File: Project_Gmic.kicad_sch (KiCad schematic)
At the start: 33 parts, among them J1 USB4085-GF-A, J2 SJ1-3523N, SW1 PCM12SMTR, T1 ESMIT-4180/C, U1 TC1055, U2 R05CTE05S

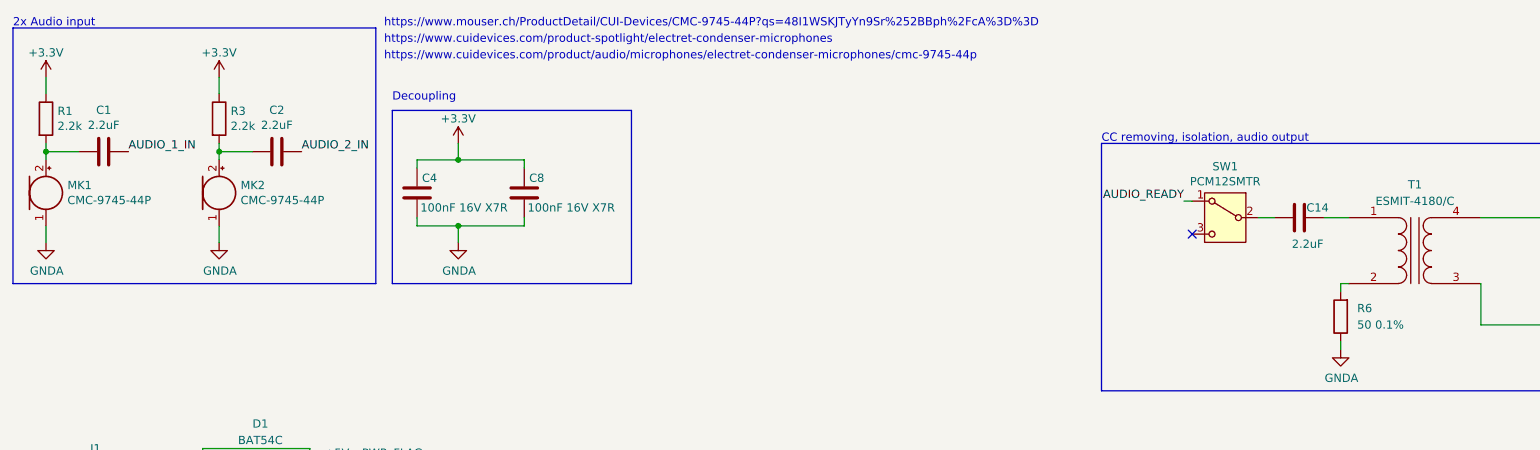
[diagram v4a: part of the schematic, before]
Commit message: placement, BOM inside kicad
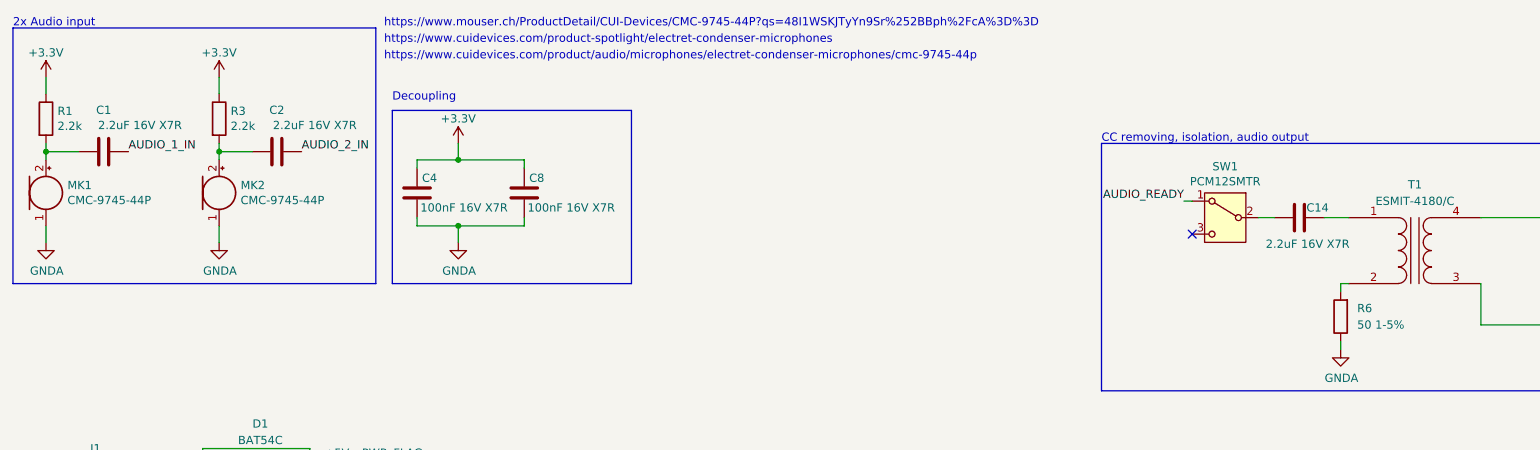
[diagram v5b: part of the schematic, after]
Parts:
- C1, C14, C2: value 2.2uF -> 2.2uF 16V X7R; Manufacturer (none) -> Samsung Electro-Mechanics; Price (none) -> 0.109; Store (none) -> Mouser; StoreID (none) -> 187-CL21B225KOFNNNE
- C10: Manufacturer (none) -> Wurth Elektronik; Price (none) -> 0.091; Store (none) -> Mouser; StoreID (none) -> 710-885012207051
- C11: Manufacturer (none) -> Wurth Elektronik; Price (none) -> 0.053; Store (none) -> Mouser; StoreID (none) -> 710-885012207045
- C12, C3: footprint (none) -> Capacitor_SMD:CP_Elec_4x5.4; Manufacturer (none) -> Wurth Elektronik; Price (none) -> 0.163; Store (none) -> Mouser; StoreID (none) -> 710-865080340001
- C13, C4, C5, C6, C8: footprint (none) -> Capacitor_SMD:C_0805_2012Metric; Manufacturer (none) -> Wurth Elektronik; Price (none) -> 0.053; Store (none) -> Mouser; StoreID (none) -> 710-885012207045
- C7, C9: footprint (none) -> Capacitor_SMD:CP_Elec_4x5.4; Manufacturer (none) -> Wurth Elektronik; Price (none) -> 0.263; Store (none) -> Mouser; StoreID (none) -> 710-865250640005
- D1: footprint Package_TO_SOT_SMD:SOT-23 -> Package_TO_SOT_SMD:SOT-23-5; Manufacturer (none) -> Panjit; Price (none) -> 0.091; Store (none) -> Mouser; StoreID (none) -> 241-BAT54C_R1_00001
- J1: footprint (none) -> Connector_USB:USB_C_Receptacle_GCT_USB4085; Manufacturer (none) -> GCT; Price (none) -> 0.898; Store (none) -> Mouser; StoreID (none) -> 640-USB4085-GF-A
- J2: Manufacturer (none) -> Same Sky; Price (none) -> 1.07; Store (none) -> Mouser; StoreID (none) -> 490-SJ1-3523N
- L1: footprint (none) -> Inductor_SMD:L_0805_2012Metric; Manufacturer (none) -> Murata Electronics; Price (none) -> 0.099; Store (none) -> Mouser; StoreID (none) -> 81-BLM21P331SG
- MK1, MK2: Manufacturer (none) -> Same Sky; Price (none) -> 0.626; Store (none) -> Mouser; StoreID (none) -> 490-CMC-9745-44P
- R1, R3: Manufacturer (none) -> YAGEO; Price (none) -> 0.091; Store (none) -> Mouser; StoreID (none) -> 603-RC0805FR-132K2L
- R2: footprint (none) -> Resistor_SMD:R_0805_2012Metric; Manufacturer (none) -> YAGEO; Price (none) -> 0.091; Store (none) -> Mouser; StoreID (none) -> 603-RC0805FR-070RL
- R4, R5: Manufacturer (none) -> Panasonic; Price (none) -> 0.091; Store (none) -> Mouser; StoreID (none) -> 667-ERJ-6ENF5101V
- R6: value 50 0.1% -> 50 1-5%; footprint (none) -> Resistor_SMD:R_0805_2012Metric; Manufacturer (none) -> YAGEO; Price (none) -> 0.091; Store (none) -> Mouser; StoreID (none) -> 603-RC0402JR-0750RL
- SW1: Manufacturer (none) -> C&K; Price (none) -> 1.02; Store (none) -> Mouser; StoreID (none) -> 611-PCM12SMTR
- T1: footprint (none) -> SOP254P914X350:SOP254P914X350-4N; Manufacturer (none) -> Sumida; Price (none) -> 1.76; Store (none) -> Mouser; StoreID (none) -> 851-ESMIT-4180/C
- U1: Manufacturer (none) -> Microchip Technology; Price (none) -> 0.445; Store (none) -> Mouser; StoreID (none) -> 579-TC1055-3.3VCT713
- U2: Manufacturer (none) -> RECOM Power; Price (none) -> 3.42; Store (none) -> Mouser; StoreID (none) -> 919-R05CTE05S-CT

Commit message: first step final
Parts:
- D1: footprint Package_TO_SOT_SMD:SOT-23-5 -> Package_TO_SOT_SMD:SOT-23
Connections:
- net USB_SHIELD: now reaches J1.S1 (SHIELD), R2.2
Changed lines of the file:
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@@
 	(title_block
 		(title "Gmic")
-		(date "2024-09-21")
+		(date "2024-10-31")
 		(rev "V1.2")
 		(company "Guillaume Guillet")
@@
 		)
 	)
+	(label "USB_SHIELD"
+		(at 19.05 125.73 270)
+		(fields_autoplaced yes)
+		(effects
+			(font
+				(size 1.27 1.27)
+			)
+			(justify right bottom)
+		)
+	)
 	(label "AUDIO_1_IN"
 		(at 170.18 92.71 180)
@@
 			)
 		)
-		(property "Footprint" "Package_TO_SOT_SMD:SOT-23-5"
+		(property "Footprint" "Package_TO_SOT_SMD:SOT-23"
 			(at 53.975 79.375 0)
 			(effects
